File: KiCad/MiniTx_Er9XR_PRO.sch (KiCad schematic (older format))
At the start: 35 parts, among them J1 CONN_01X03, J10 STAB, J11 CH5, J2 BAT2, J3 BAT1, J4 BAT, J5 LED1, J6 THRTL1, J7 MODULE1_POWER, J8 3.3V, J9 LED1, SW1 BIND, SW4 SW_DPST_x2, U1 arduino_mini, U2 MIC5219-3.3BM5, U4 MIC5219-3.3BM5, U5 arduino_mini

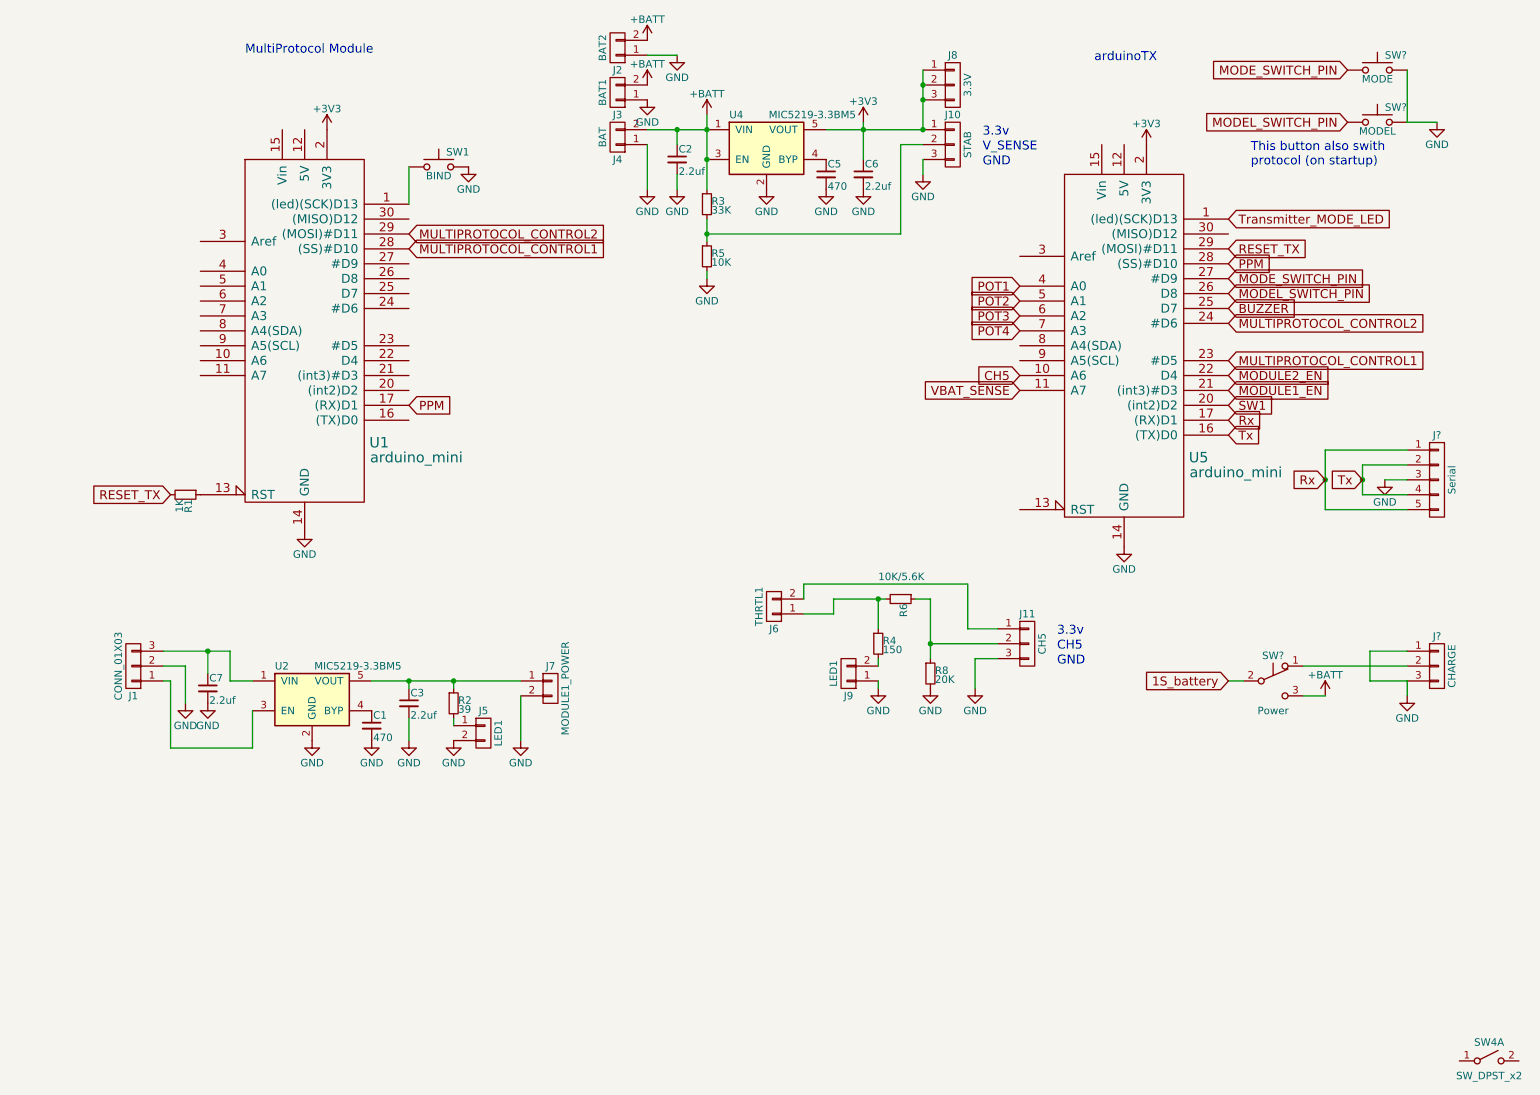
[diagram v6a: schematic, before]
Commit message: Adjust schematic to have correct pin mapping
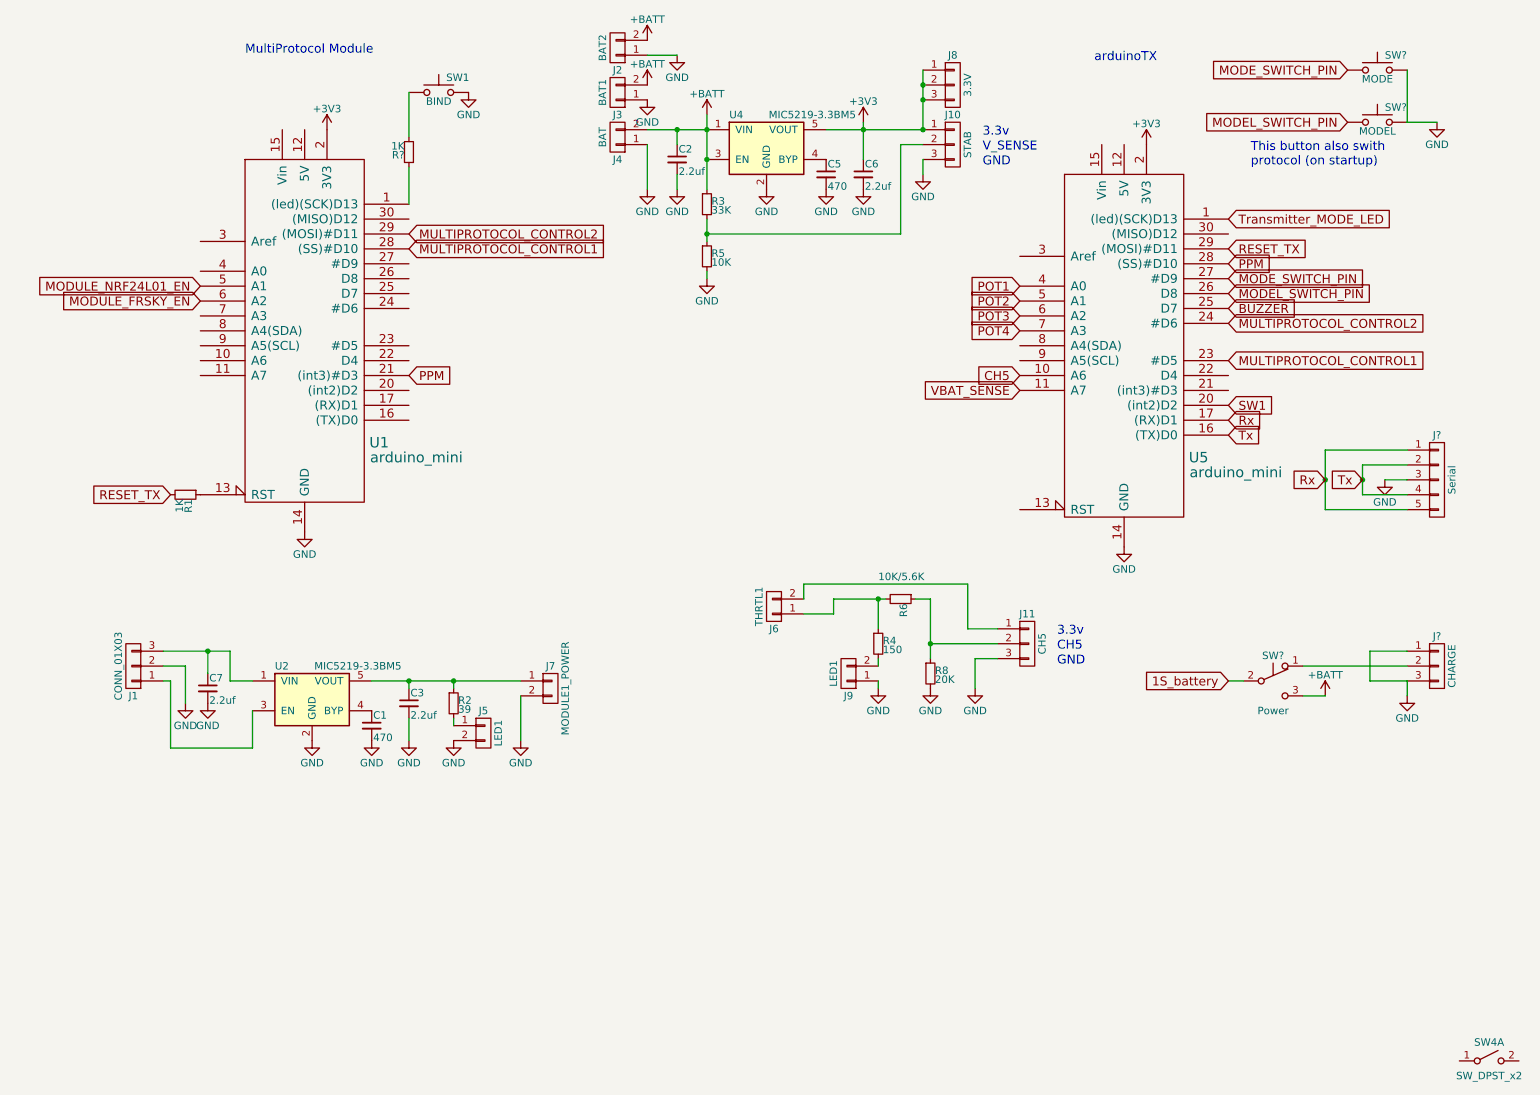
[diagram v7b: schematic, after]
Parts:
- added R?: 1K, symbol R_Small
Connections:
- net PPM: now also U1.21 ((int3)#D3); no longer U1.17 ((RX)D1)
- net at U1.1 ((led)(SCK)D13): now also R?.1; no longer SW1.1
- net MODULE_NRF24L01_EN: now reaches U1.5 (A1)
- net MODULE_FRSKY_EN: now reaches U1.6 (A2)
- net MODULE1_EN: no longer names the net of U5.21 ((int3)#D3)
- net MODULE2_EN: no longer names the net of U5.22 (D4)
- new net: R?.2, SW1.1
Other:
- moved on the sheet: SW1
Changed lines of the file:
@@
 Text GLabel 8750 3350 2    60   Input ~ 0
 SW1
-Text GLabel 8750 3250 2    60   Input ~ 0
-MODULE1_EN
-Text GLabel 8750 3150 2    60   Input ~ 0
-MODULE2_EN
+Text GLabel 1850 2550 0    60   Input ~ 0
+MODULE_NRF24L01_EN
+Text GLabel 1850 2650 0    60   Input ~ 0
+MODULE_FRSKY_EN
 Text GLabel 8750 3050 2    60   Input ~ 0
 MULTIPROTOCOL_CONTROL1
@@
 $EndComp
 Wire Wire Line
-	6750 4650 6750 4950
-Wire Wire Line
-	6750 4950 6750 5050
+	6750 4650 6750 5050
 Connection ~ 6750 4950
 $Comp
@@
 L SW_Push SW1
 U 1 1 59081423
-P 3450 1750
-F 0 "SW1" H 3500 1850 50  0000 L CNN
-F 1 "BIND" H 3450 1690 50  0000 C CNN
-F 2 "" H 3450 1950 50  0001 C CNN
-F 3 "" H 3450 1950 50  0001 C CNN
-	1    3450 1750
+P 3450 1250
+F 0 "SW1" H 3500 1350 50  0000 L CNN
+F 1 "BIND" H 3450 1190 50  0000 C CNN
+F 2 "" H 3450 1450 50  0001 C CNN
+F 3 "" H 3450 1450 50  0001 C CNN
+	1    3450 1250
 	1    0    0    -1
 $EndComp
@@
 L GND #PWR09
 U 1 1 590815B2
-P 3650 1750
-F 0 "#PWR09" H 3650 1500 50  0001 C CNN
-F 1 "GND" H 3650 1600 50  0000 C CNN
-F 2 "" H 3650 1750 50  0001 C CNN
-F 3 "" H 3650 1750 50  0001 C CNN
-	1    3650 1750
-	1    0    0    -1
-$EndComp
-Text GLabel 3250 3350 2    60   Input ~ 0
+P 3650 1250
+F 0 "#PWR09" H 3650 1000 50  0001 C CNN
+F 1 "GND" H 3650 1100 50  0000 C CNN
+F 2 "" H 3650 1250 50  0001 C CNN
+F 3 "" H 3650 1250 50  0001 C CNN
+	1    3650 1250
+	1    0    0    -1
+$EndComp
+Text GLabel 3250 3150 2    60   Input ~ 0
 PPM
 $Comp
@@
 $EndComp
 Wire Wire Line
-	3000 5200 3250 5200
-Wire Wire Line
-	3250 5200 3550 5200
-Wire Wire Line
-	3550 5200 4000 5200
+	3000 5200 4000 5200
 $Comp
 L GND #PWR010
@@
 $EndComp
 Wire Wire Line
-	5250 1400 5250 1500
-Wire Wire Line
-	5250 1500 5250 1700
-Wire Wire Line
-	5250 1700 5250 1900
-Wire Wire Line
-	6700 1500 6300 1500
-Wire Wire Line
-	6300 1500 6050 1500
+	5250 1400 5250 1900
+Wire Wire Line
+	6700 1500 6050 1500
 $Comp
 L CONN_01X02 J5
@@
 	6650 4650 6750 4650
 Wire Wire Line
-	6100 4650 6400 4650
-Wire Wire Line
-	6400 4650 6450 4650
+	6100 4650 6450 4650
 $Comp
 L CONN_01X02 J9
@@
 $EndComp
 Wire Wire Line
-	1600 5000 1900 5000
-Wire Wire Line
-	1900 5000 2050 5000
+	1600 5000 2050 5000
 Wire Wire Line
 	3550 5250 3550 5200
@@
 Connection ~ 5250 1700
 Wire Wire Line
-	5250 2100 5250 2200
-Wire Wire Line
-	5250 2200 5250 2250
+	5250 2100 5250 2250
 Wire Wire Line
 	5250 2500 5250 2450
@@
 $EndComp
 Wire Wire Line
-	4850 1500 5050 1500
-Wire Wire Line
-	5050 1500 5250 1500
+	4850 1500 5250 1500
 $Comp
 L GND #PWR022
@@
 Connection ~ 5250 1500
 Wire Wire Line
-	6300 1450 6300 1500
-Wire Wire Line
-	6300 1500 6300 1700
+	6300 1450 6300 1700
 Connection ~ 6300 1500
 $Comp
@@
 $EndComp
 Wire Wire Line
-	6700 1100 6700 1200
-Wire Wire Line
-	6700 1200 6700 1300
-Wire Wire Line
-	6700 1300 6700 1500
+	6700 1100 6700 1500
 Connection ~ 6700 1200
 Connection ~ 6700 1300
@@
 	9950 3750 9650 3750
 Wire Wire Line
-	9650 3750 9650 3850
-Wire Wire Line
-	9650 3850 9650 3950
+	9650 3750 9650 3950
 Wire Wire Line
 	9650 3950 9950 3950
 Wire Wire Line
-	9950 4050 9400 4050
-Wire Wire Line
-	9400 4050 9400 3850
-Wire Wire Line
-	9400 3850 9400 3650
+	9400 4050 9950 4050
+Wire Wire Line
+	9400 3650 9400 4050
 Wire Wire Line
 	9400 3650 9950 3650
 Connection ~ 9650 3850
 Connection ~ 9400 3850
+$Comp
+L R_Small R?
+U 1 1 592C708D
+P 3250 1650
+F 0 "R?" H 3280 1670 50  0000 L CNN
+F 1 "1K" H 3280 1610 50  0000 L CNN
+F 2 "" H 3250 1650 50  0001 C CNN
+F 3 "" H 3250 1650 50  0001 C CNN
+	1    3250 1650
+	-1   0    0    1
+$EndComp
+Wire Wire Line
+	3250 1550 3250 1250
 $EndSCHEMATC
